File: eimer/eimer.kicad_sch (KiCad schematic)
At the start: 33 parts, among them J1 Conn_01x20, J2 Conn_01x20, J3 Conn_01x03, J4 USB_C_Receptacle_USB2.0_14P, SW1 SW_Push, U1 RP2040, U2 MCP1700x-330xxTT, U4 W25Q16JVUXIQ TR, Y1 12 MHz

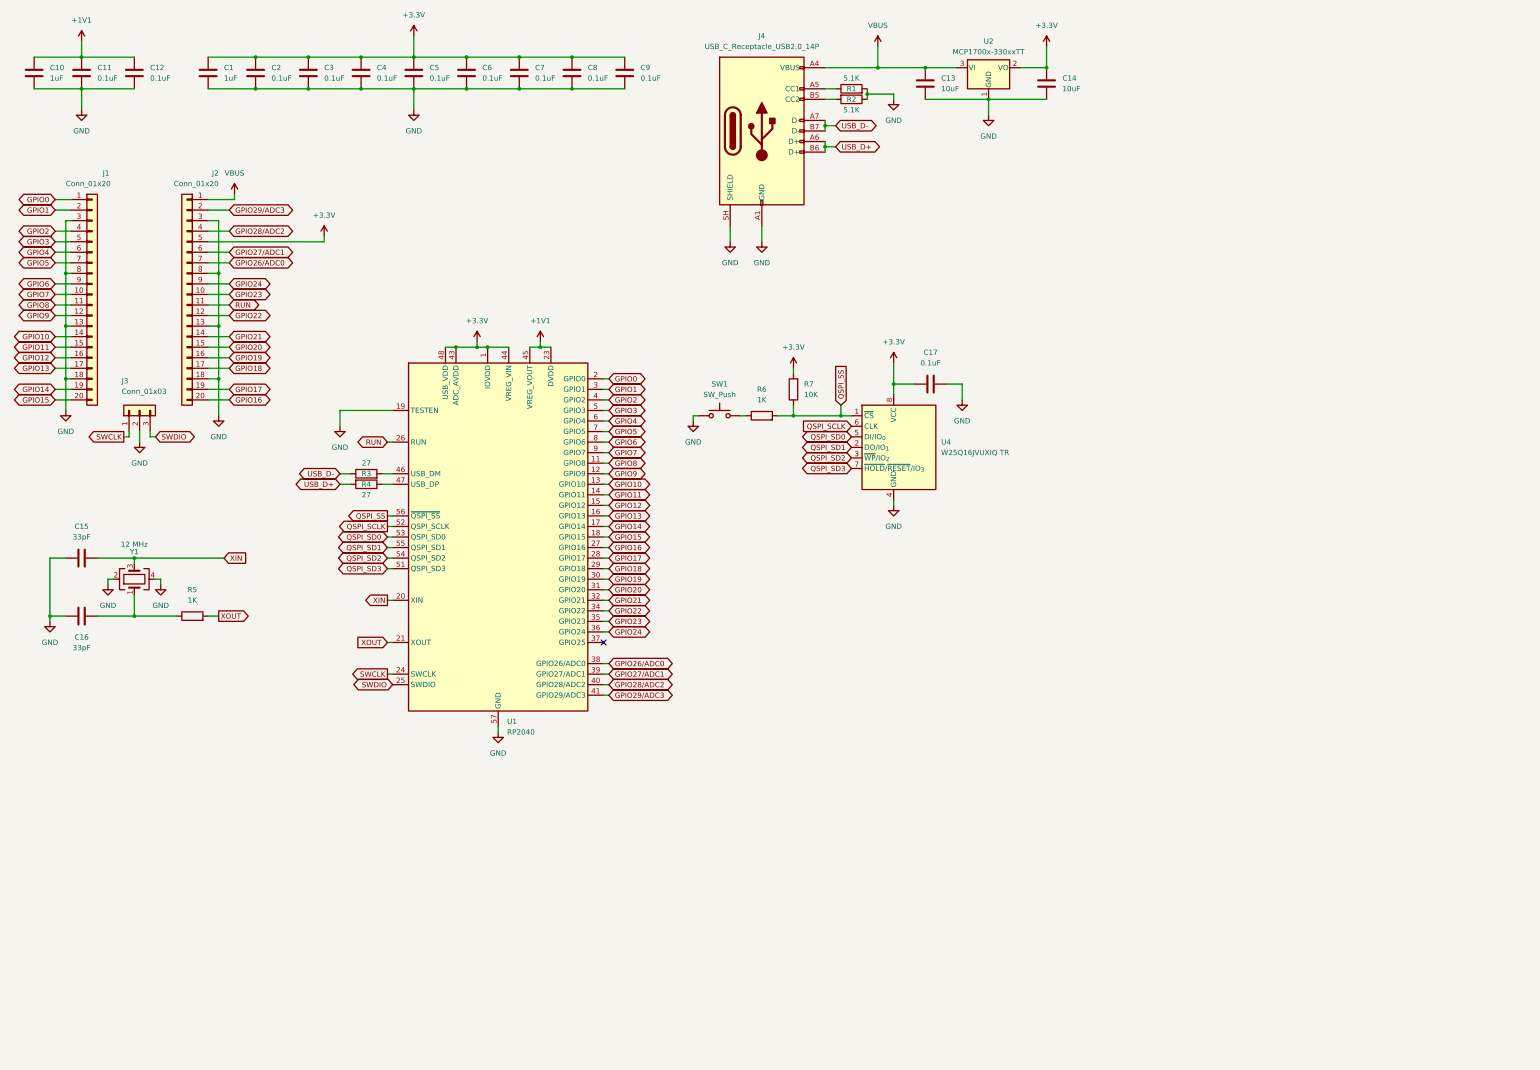
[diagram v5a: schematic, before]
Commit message: finished schematic for wearable mcu
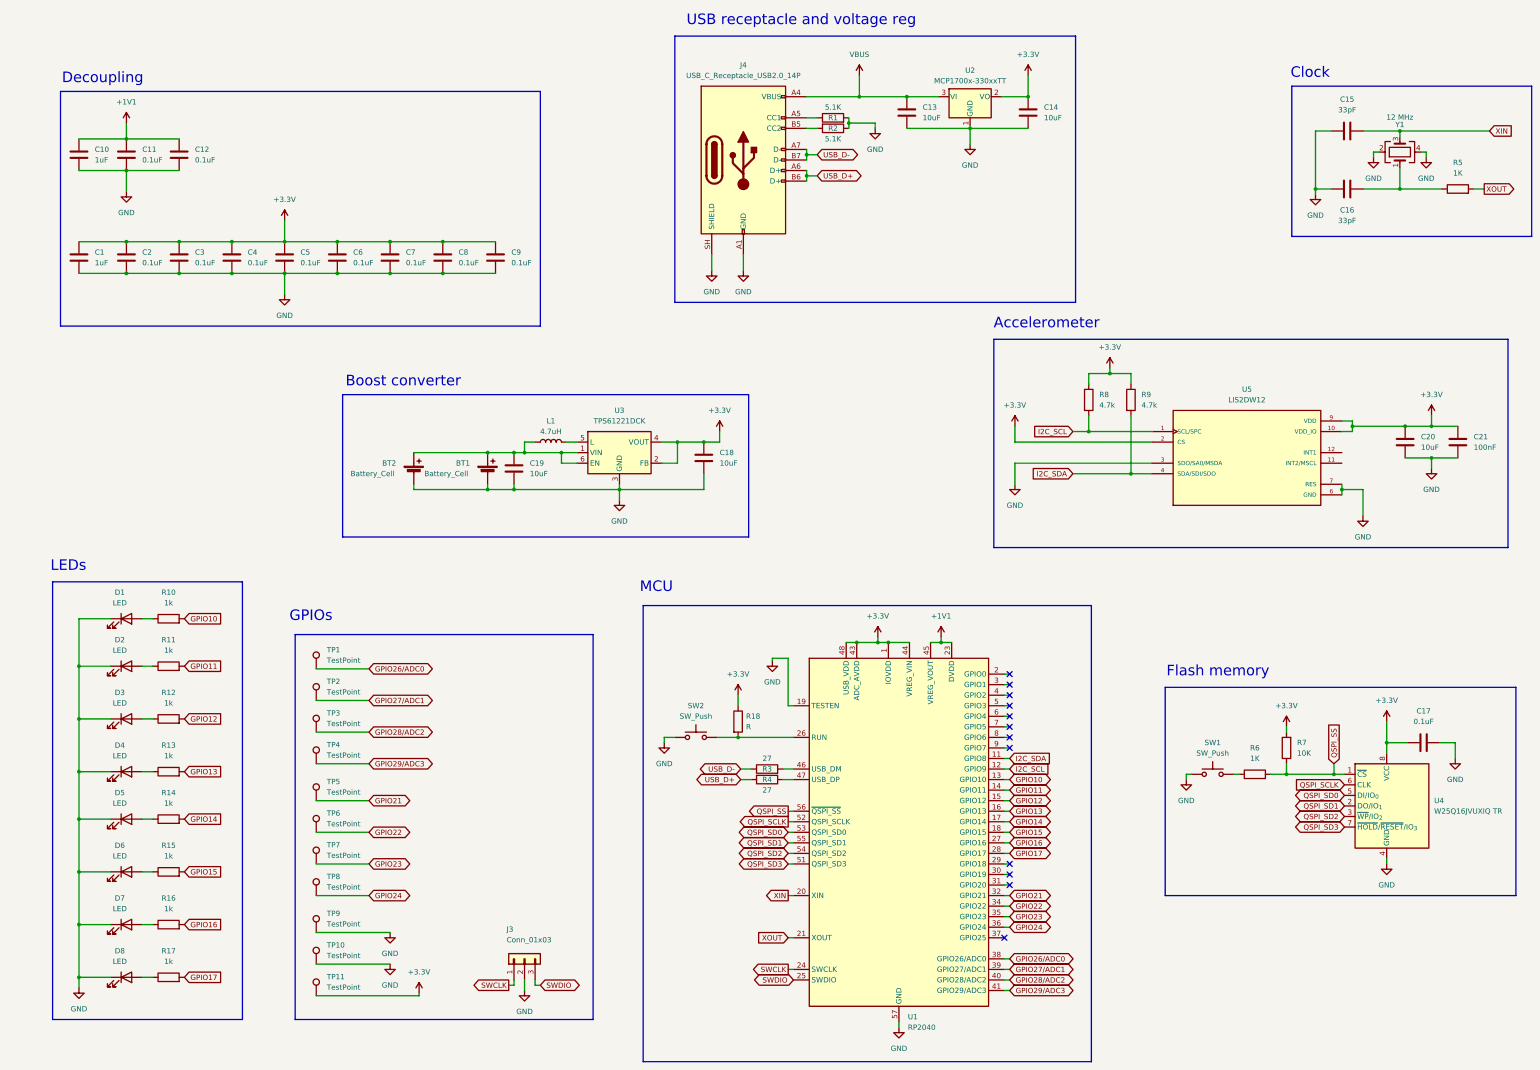
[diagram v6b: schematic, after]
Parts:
- removed J1, J2: Conn_01x20, Connector_PinHeader_2.54mm:PinHeader_1x20_P2.54mm_Vertical, symbol Connector_Generic:Conn_01x20
- added BT1, BT2: Battery_Cell, symbol Device:Battery_Cell
- added C18, C19, C20: 10uF, symbol Device:C
- added C21: 100nF, symbol Device:C
- added D1, D2, D3, D4, D5, D6, D7, D8: LED, symbol Device:LED
- added L1: 4.7uH, symbol Device:L
- added R10, R11, R12, R13, R14, R15, R16, R17: 1k, symbol Device:R
- added R18: R, symbol Device:R
- added R8, R9: 4.7k, symbol Device:R
- added SW2: SW_Push, Button_Switch_SMD:SW_Push_SPST_NO_Alps_SKRK, symbol Switch:SW_Push
- added TP1, TP10, TP11, TP2, TP3, TP4, TP5, TP6, TP7, TP8, TP9: TestPoint, symbol Connector:TestPoint
- added U3: TPS61221DCK, Package_TO_SOT_SMD:Texas_R-PDSO-G6, symbol Regulator_Switching:TPS61221DCK
- added U5: LIS2DW12, LIS2DS12:LIS2DS12, symbol LIS2DS12:LIS2DS12
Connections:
- net +3.3V: now also C18.1, C20.1, C21.1, R18.1, R8.1, R9.1, TP11.1, U3.2 (FB), U3.4 (VOUT), U5.10 (VDD_IO), U5.2 (CS), U5.9 (VDD)
- net GND: now also BT1.2 (-), BT2.2 (-), C18.2, C19.2, C20.2, C21.2, D1.1 (K), D2.1 (K), D3.1 (K), D4.1 (K), D5.1 (K), D6.1 (K), D7.1 (K), D8.1 (K), SW2.1, TP10.1, TP9.1, U3.3 (GND), U5.3 (SDO/SA0/MSDA), U5.6 (GND), U5.7 (RES), U5.8 (GND)
- net GPIO10: now also R10.2
- net GPIO11: now also R11.2
- net GPIO12: now also R12.2
- net GPIO13: now also R13.2
- net GPIO14: now also R14.2
- net GPIO15: now also R15.2
- net GPIO16: now also R16.2
- net GPIO17: now also R17.2
- net GPIO21: now also TP5.1
- net GPIO22: now also TP6.1
- net GPIO23: now also TP7.1
- net GPIO24: now also TP8.1
- net GPIO26/ADC0: now also TP1.1
- net GPIO27/ADC1: now also TP2.1
- net GPIO28/ADC2: now also TP3.1
- net GPIO29/ADC3: now also TP4.1
- net GPIO0: no longer names the net of U1.2 (GPIO0)
- net GPIO1: no longer names the net of U1.3 (GPIO1)
- net GPIO18: no longer names the net of U1.29 (GPIO18)
- net GPIO19: no longer names the net of U1.30 (GPIO19)
- net GPIO2: no longer names the net of U1.4 (GPIO2)
- net GPIO20: no longer names the net of U1.31 (GPIO20)
- net GPIO3: no longer names the net of U1.5 (GPIO3)
- net GPIO4: no longer names the net of U1.6 (GPIO4)
- net GPIO5: no longer names the net of U1.7 (GPIO5)
- net GPIO6: no longer names the net of U1.8 (GPIO6)
- net GPIO7: no longer names the net of U1.9 (GPIO7)
- net GPIO8 renamed I2C_SDA
- net I2C_SDA: now also R9.2, U5.4 (SDA/SDI/SDO)
- net GPIO9 renamed I2C_SCL
- net I2C_SCL: now also R8.2, U5.1 (SCL/SPC)
- net RUN: no longer names the net of U1.26 (RUN)
- net RUN: now also R18.2, SW2.2
- new net: BT1.1 (+), BT2.1 (+), C19.1, L1.1, U3.1 (VIN), U3.6 (EN)
- new net: D5.2 (A), R14.1
- new net: D8.2 (A), R17.1
- new net: D7.2 (A), R16.1
- new net: D4.2 (A), R13.1
- new net: D3.2 (A), R12.1
- new net: D6.2 (A), R15.1
- new net: D2.2 (A), R11.1
- new net: D1.2 (A), R10.1
- new net: L1.2, U3.5 (L)
- no-connect marks 1 -> 12
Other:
- note added: "Accelerometer"
- note added: "Boost converter"
- note added: "Clock"
- note added: "Decoupling"
- note added: "Flash memory"
- note added: "GPIOs"
- note added: "LEDs"
- note added: "MCU"
- note added: "USB receptacle and voltage reg"
- title: (none) -> Eimer
- moved on the sheet: C1, C10, C11, C12, C13, C14, C15, C16, C17, C2, C3, C4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

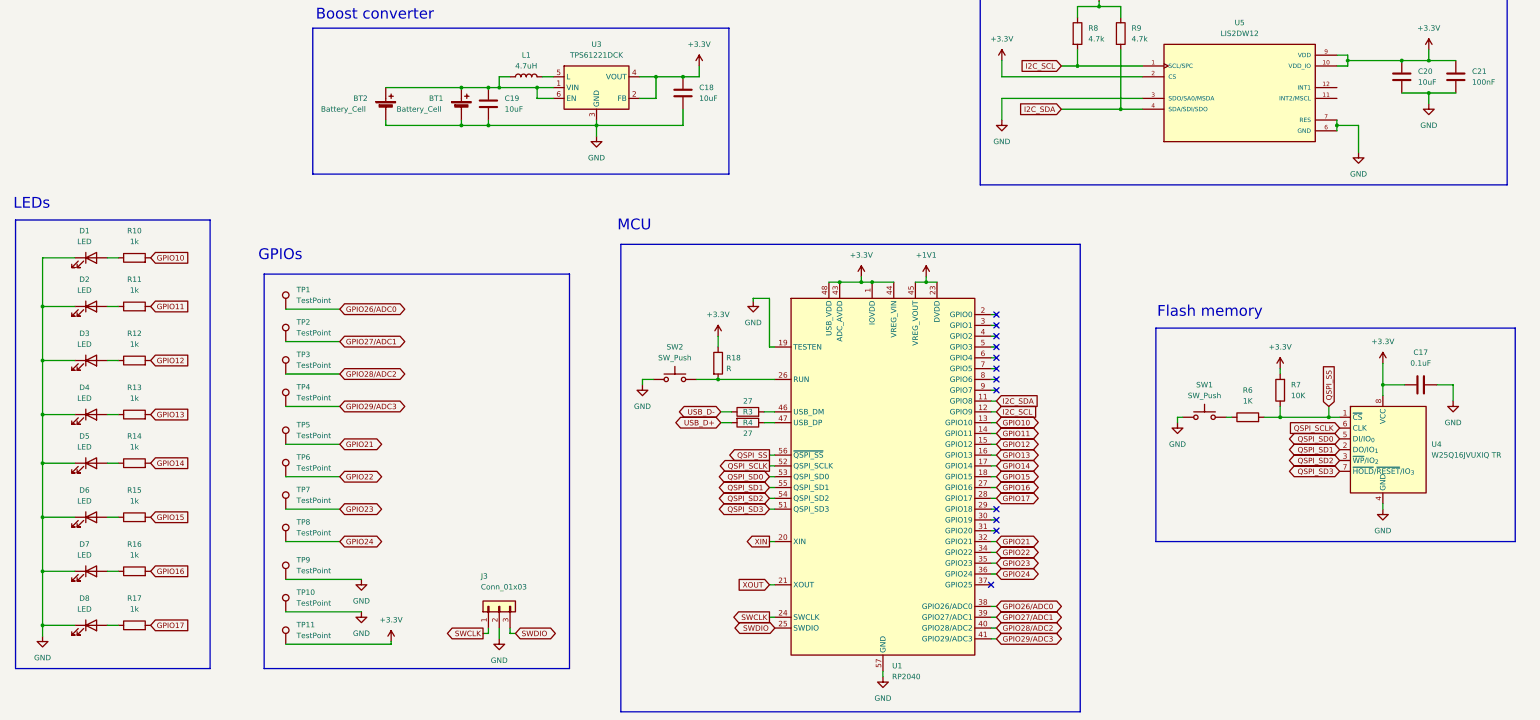
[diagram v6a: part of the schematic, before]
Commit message: assigned footprints
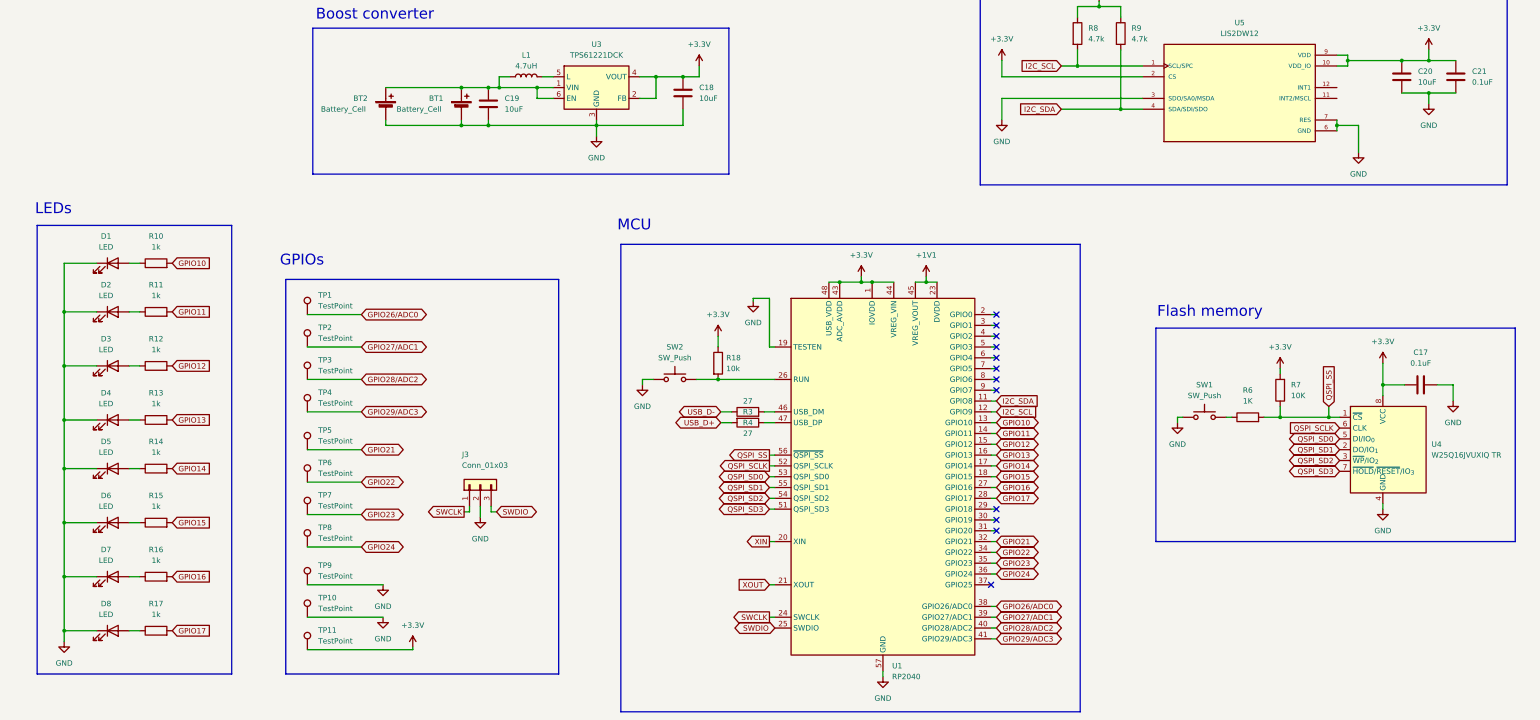
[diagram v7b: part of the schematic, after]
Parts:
- BT1, BT2: footprint (none) -> Battery:BatteryHolder_Multicomp_BC-2001_1x2032
- C18, C19, C20: footprint (none) -> Capacitor_SMD:C_0603_1608Metric
- C21: value 100nF -> 0.1uF; footprint (none) -> Capacitor_SMD:C_0402_1005Metric
- D1, D2, D3, D4, D5, D6, D7, D8: footprint (none) -> LED_SMD:LED_0201_0603Metric
- L1: footprint (none) -> Inductor_SMD:L_APV_ANR3015
- R10, R11, R12, R13, R14, R15, R16, R17, R8, R9: footprint (none) -> Resistor_SMD:R_0402_1005Metric
- R18: value R -> 10k; footprint (none) -> Resistor_SMD:R_0402_1005Metric
- TP1, TP10, TP11, TP2, TP3, TP4, TP5, TP6, TP7, TP8, TP9: footprint (none) -> TestPoint:TestPoint_THTPad_D1.5mm_Drill0.7mm
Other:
- moved on the sheet: D1, D2, D3, D4, D5, D6, D7, D8, J3, R10, R11, R12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
